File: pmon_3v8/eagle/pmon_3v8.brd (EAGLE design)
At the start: 60 x 60 mm, 34 parts, among them J1 USB, J2 USB, J4 PINHD-1X3, J5 PINHD-2X3, Q1 16Mhz, U1 LTC2943, U2 FT232RL, U3 LT1764AEQ, U4 ATMEGA328TQFP32

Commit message: Renamed power play oled to power play 3.8V (to be consistent with the 5V name of the other variant).
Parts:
- SB1: device pmon_oled:JUMPER_SOLDER_1X2 -> pmon_3v8:JUMPER_SOLDER_1X2
- U1: device pmon_oled:DFN8-3X3 -> pmon_3v8:DFN8-3X3
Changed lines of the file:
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@@
 <attribute name="NAME" x="52.905325" y="19.074971875" size="1.016" layer="25" font="vector" ratio="10" rot="R180"/>
 </element>
-<element name="U1" library="pmon_oled" package="DFN8-3X3" value="LTC2943" x="45.974" y="13.208" smashed="yes" rot="R180">
+<element name="U1" library="pmon_3v8" package="DFN8-3X3" value="LTC2943" x="45.974" y="13.208" smashed="yes" rot="R180">
 <attribute name="NAME" x="45.68035625" y="11.32620625" size="1.016" layer="25" font="vector" ratio="10" rot="R180"/>
 </element>
@@
 <attribute name="NAME" x="18.914784375" y="46.715384375" size="1.016" layer="25" font="vector" ratio="10"/>
 </element>
-<element name="SB1" library="pmon_oled" package="JUMPER_SOLDER_1X2" value="JUMPER_SOLDER_1X2" x="9.525" y="36.91" smashed="yes">
+<element name="SB1" library="pmon_3v8" package="JUMPER_SOLDER_1X2" value="JUMPER_SOLDER_1X2" x="9.525" y="36.91" smashed="yes">
 <attribute name="NAME" x="8.3742625" y="38.280121875" size="1.016" layer="25" font="vector" ratio="10" rot="SR0"/>
 </element>

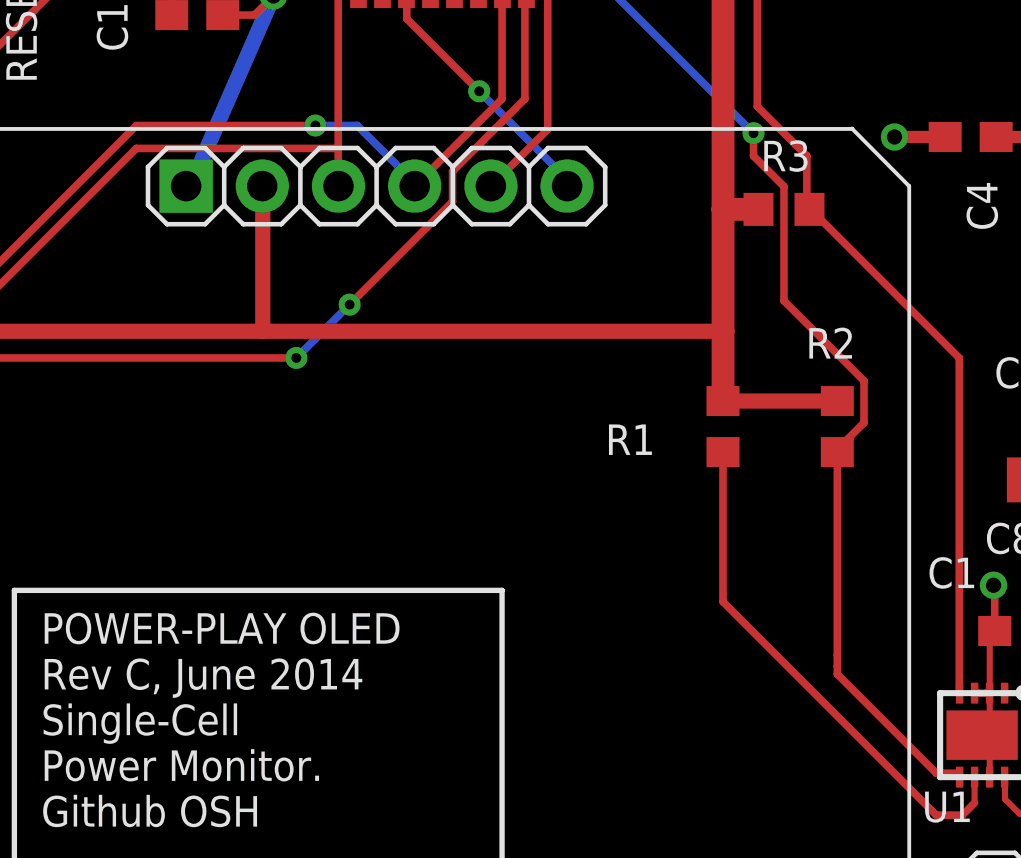
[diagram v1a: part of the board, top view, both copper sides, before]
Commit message: Added OLED reset pull down resistor.
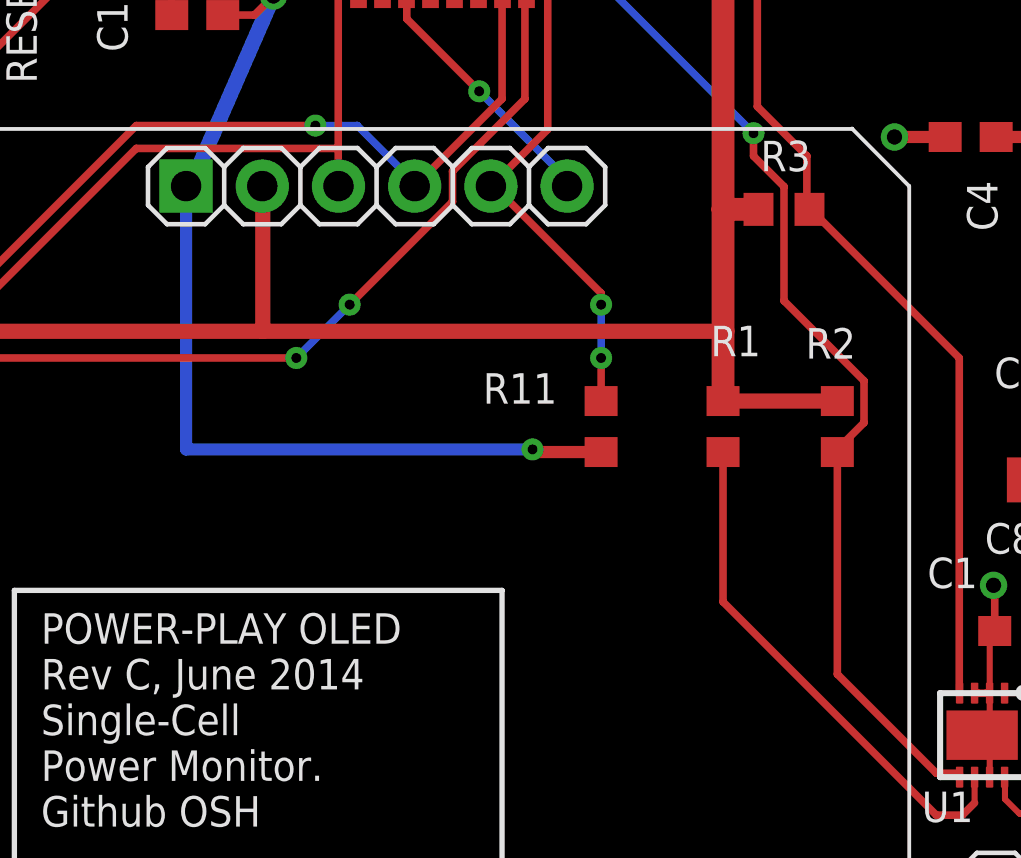
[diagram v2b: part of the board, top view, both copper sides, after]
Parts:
- added R11: 3K3, pmon_3v8:R0603
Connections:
- net GND: now also R11.1
- net OLED_RST: now also R11.2
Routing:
- net GND: track 120.5 -> 143.2 mm, vias 31 -> 32
- net OLED_RST: track 14.6 -> 23.3 mm, vias 0 -> 2
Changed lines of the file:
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@@
 </element>
 <element name="R1" library="pmon_oled" package="R0603" value="3K3" x="37.338" y="23.495" smashed="yes" rot="R90">
-<attribute name="NAME" x="35.082921875" y="23.564084375" size="1.016" layer="25" font="vector" ratio="10" rot="R180"/>
+<attribute name="NAME" x="36.926078125" y="25.838915625" size="1.016" layer="25" font="vector" ratio="10"/>
 </element>
 <element name="J2" library="pmon_oled" package="USB-MICRO-ZX62RD-AB-5P8" value="USB" x="18" y="60.5" smashed="yes" rot="R180">
@@
 <element name="S1" library="pmon_oled" package="TLE1105" value="PUSH_BUTTON" x="4.2977375" y="16.99769375" smashed="yes">
 <attribute name="NAME" x="3.37514375" y="11.875646875" size="1.016" layer="25" font="vector" ratio="10"/>
+</element>
+<element name="R11" library="pmon_3v8" package="R0603" value="3K3" x="33.274" y="23.495" smashed="yes" rot="R90">
+<attribute name="NAME" x="29.337" y="24.257" size="1.016" layer="25" font="vector" ratio="10"/>
 </element>
 </elements>
@@
 <wire x1="45.085" y1="52.705" x2="45.085" y2="49.911" width="1.27" layer="1"/>
 <wire x1="45.085" y1="49.911" x2="45.466" y2="49.53" width="0.4064" layer="1"/>
+<contactref element="R11" pad="1"/>
+<wire x1="33.274" y1="22.645" x2="30.988" y2="22.645" width="0.4064" layer="1"/>
+<wire x1="30.988" y1="22.645" x2="30.988" y2="22.733" width="0.4064" layer="1"/>
+<via x="30.988" y="22.733" extent="1-16" drill="0.3302"/>
+<wire x1="30.988" y1="22.733" x2="19.44" y2="22.733" width="0.4064" layer="16"/>
+<wire x1="19.44" y1="22.733" x2="19.44" y2="31.51" width="0.4064" layer="16"/>
 </signal>
 <signal name="+5V">
@@
 <contactref element="U4" pad="27"/>
 <wire x1="44.45" y1="11.938" x2="45.212" y2="11.938" width="0.254" layer="1"/>
-<wire x1="41.148" y1="22.645" x2="41.148" y2="15.875" width="0.254" layer="1"/>
-<wire x1="41.148" y1="15.875" x2="41.148" y2="15.494" width="0.254" layer="1"/>
+<wire x1="41.148" y1="22.645" x2="41.148" y2="15.24" width="0.254" layer="1"/>
 <wire x1="45.212" y1="11.938" x2="45.224" y2="11.808" width="0.254" layer="1"/>
 <wire x1="29.21" y1="45.212" x2="29.21" y2="46.609" width="0.254" layer="1"/>
@@
 <via x="38.354" y="33.274" extent="1-16" drill="0.3302"/>
 <wire x1="44.45" y1="11.938" x2="41.148" y2="15.24" width="0.254" layer="1"/>
-<wire x1="41.148" y1="15.24" x2="41.148" y2="15.494" width="0.254" layer="1"/>
 </signal>
 <signal name="N$18">
@@
 <wire x1="26.035" y1="38.1" x2="25.987" y2="38.0784" width="0.254" layer="1"/>
 <wire x1="29.718" y1="31.623" x2="29.6" y2="31.51" width="0.254" layer="1"/>
+<contactref element="R11" pad="2"/>
+<wire x1="33.274" y1="25.781" x2="33.274" y2="24.345" width="0.254" layer="1"/>
+<wire x1="33.274" y1="27.559" x2="33.274" y2="25.781" width="0.254" layer="16"/>
+<wire x1="33.274" y1="27.94" x2="33.274" y2="27.559" width="0.254" layer="1"/>
+<wire x1="29.718" y1="31.496" x2="33.274" y2="27.94" width="0.254" layer="1"/>
+<wire x1="29.718" y1="31.496" x2="29.6" y2="31.51" width="0.254" layer="1"/>
+<via x="33.274" y="25.781" extent="1-16" drill="0.3302"/>
+<via x="33.274" y="27.559" extent="1-16" drill="0.3302"/>
 </signal>
 <signal name="MISO">

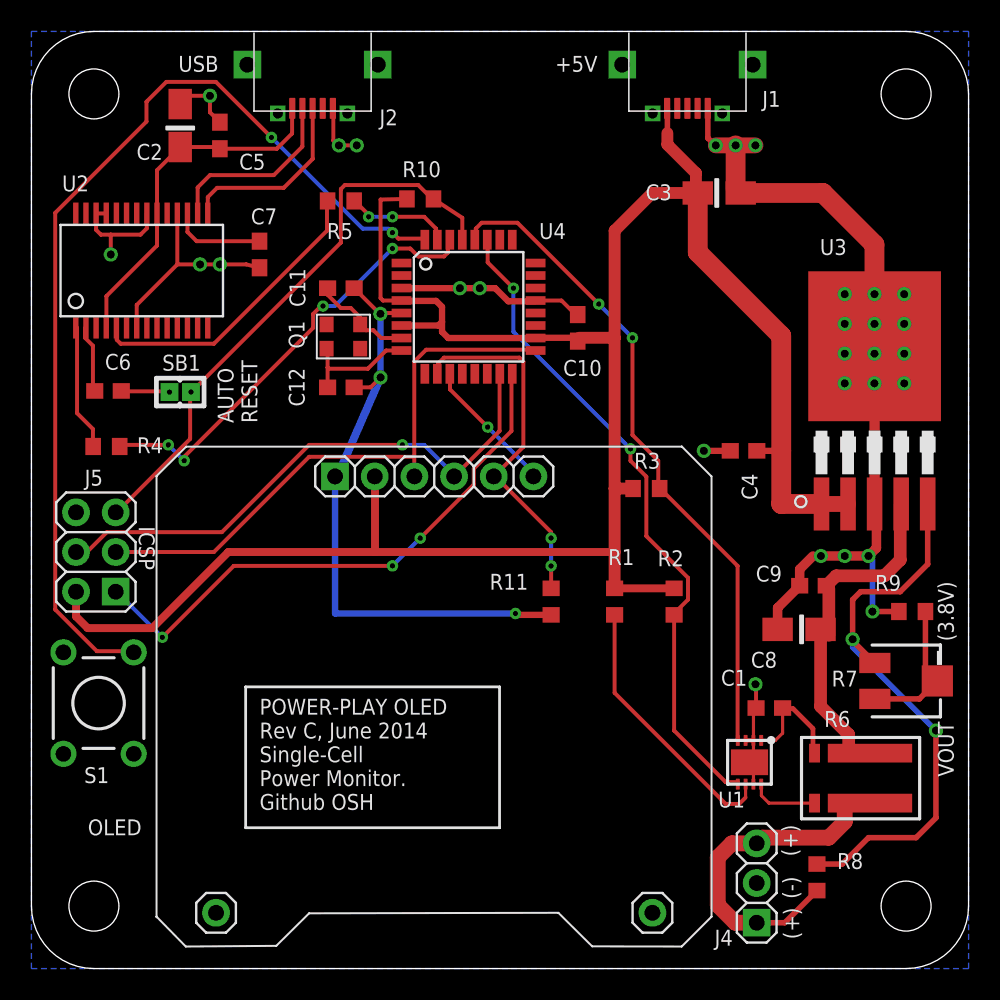
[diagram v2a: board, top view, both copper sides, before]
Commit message: Added 4V regulator. Yet to do final auto routing.
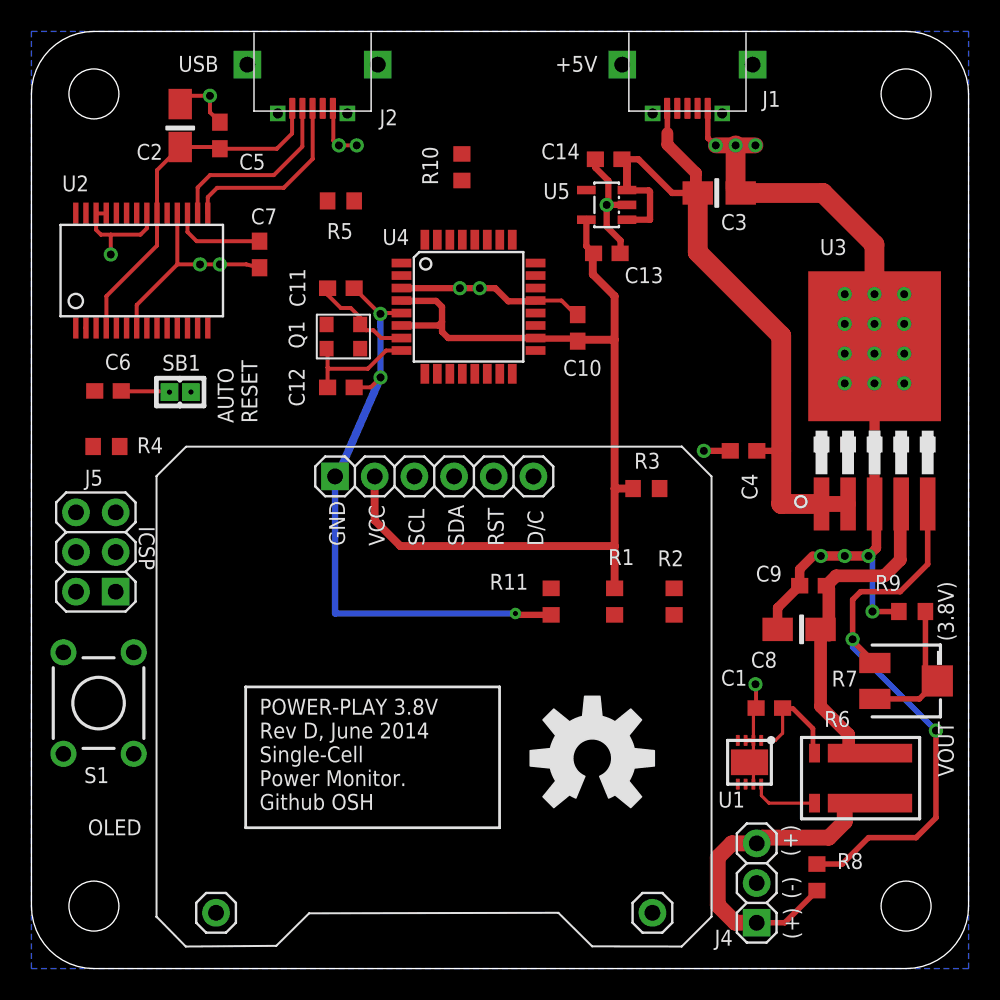
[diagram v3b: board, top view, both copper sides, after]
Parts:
- added C13, C14: 1uF, pmon_3v8:C0603
- added U$28: OSH, pmon_3v8:OSH
- added U5: TC1015, pmon_3v8:SOT25
- OLED: device pmon_oled:OLED -> pmon_3v8:OLED
- moved R10 3.35 mm to (27.6, 51.3), turned to 90 degrees
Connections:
- new net +4V: C10.1, C13.1, J5.2, OLED.2, R1.2, R10.2, R2.2, R3.2, U4.18, U4.4, U4.6, U5.5
- net +5V: now also C14.1, U5.1, U5.3; no longer C10.1, J5.2, OLED.2, R1.2, R10.2, R2.2, R3.2, U4.18, U4.4, U4.6
- net GND: now also C13.2, C14.2, U5.2
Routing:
- net +5V: track 143.7 -> 50.9 mm
- net START: track 63.6 -> 0.00 mm, vias 2 -> 0
- net +4V: track 0.00 -> 62.9 mm
- net I2C-DATA: track 42.7 -> 0.00 mm, vias 2 -> 0
- net I2C-CLK: track 42.6 -> 0.00 mm, vias 2 -> 0
- net SCK: track 37.2 -> 0.13 mm
- net RESET: track 36.8 -> 0.02 mm
- net MISO: track 36.3 -> 0.00 mm, vias 3 -> 0
- net MOSI: track 35.7 -> 0.00 mm, vias 1 -> 0
- net SER_RX: track 29.0 -> 0.00 mm, vias 4 -> 0
- net OLED_RST: track 23.3 -> 0.00 mm, vias 2 -> 0
- net N$8: track 19.3 -> 0.00 mm
- net N$1: track 17.4 -> 0.00 mm
- net OLED_D/C: track 8.88 -> 0.00 mm, vias 1 -> 0
- net N$6: track 8.10 -> 0.00 mm
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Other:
- board text added: "POWER-PLAY 3.8V - REV D OSH GITHUB"
- board text added: "POWER-PLAY 3.8V Rev D, June 2014 Single-Cell Power Monitor. Github OSH"
- board text removed: "POWER-PLAY OLED - REV C OSH GITHUB"
- board text removed: "POWER-PLAY OLED Rev C, June 2014 Single-Cell Power Monitor. Github OSH"

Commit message: Performed final routing.
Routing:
- net SER_RX: track 0.00 -> 45.8 mm, vias 0 -> 2
- net START: track 0.00 -> 43.9 mm, vias 0 -> 2
- net I2C-CLK: track 0.00 -> 42.6 mm, vias 0 -> 2
- net I2C-DATA: track 0.00 -> 42.5 mm, vias 0 -> 2
- net MOSI: track 0.00 -> 37.7 mm
- net SCK: track 0.13 -> 37.5 mm
- net +4V: track 62.9 -> 99.0 mm
- net RESET: track 0.02 -> 35.6 mm
- net MISO: track 0.00 -> 33.9 mm, vias 0 -> 2
- net OLED_RST: track 0.00 -> 23.3 mm, vias 0 -> 2
- net N$8: track 0.00 -> 19.5 mm
- net N$1: track 0.00 -> 16.2 mm
- net OLED_D/C: track 0.00 -> 8.88 mm, vias 0 -> 1
- net N$6: track 0.00 -> 8.10 mm
- net SER_TX: track 0.00 -> 6.72 mm
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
